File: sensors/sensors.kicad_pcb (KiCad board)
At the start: 2 copper layers, 75 x 56 mm, 69 parts, among them J1 GPIO, J3 JP_PWM, J4 JP_ADC, J5 JP_GPS, J6 JP_RADIO, J7 JP_RCIN, SW1 SW_SPDT_321, U1 SC16IS752IPW, U2 PCA9685PW, U3 ICM-42605, U4 IST8310, U5 MS5611-01BA, U6 74LVC1G86, U7 ADS1115IDGS, Y1 14.7456MHz, Y2 ASE-xxxMHz

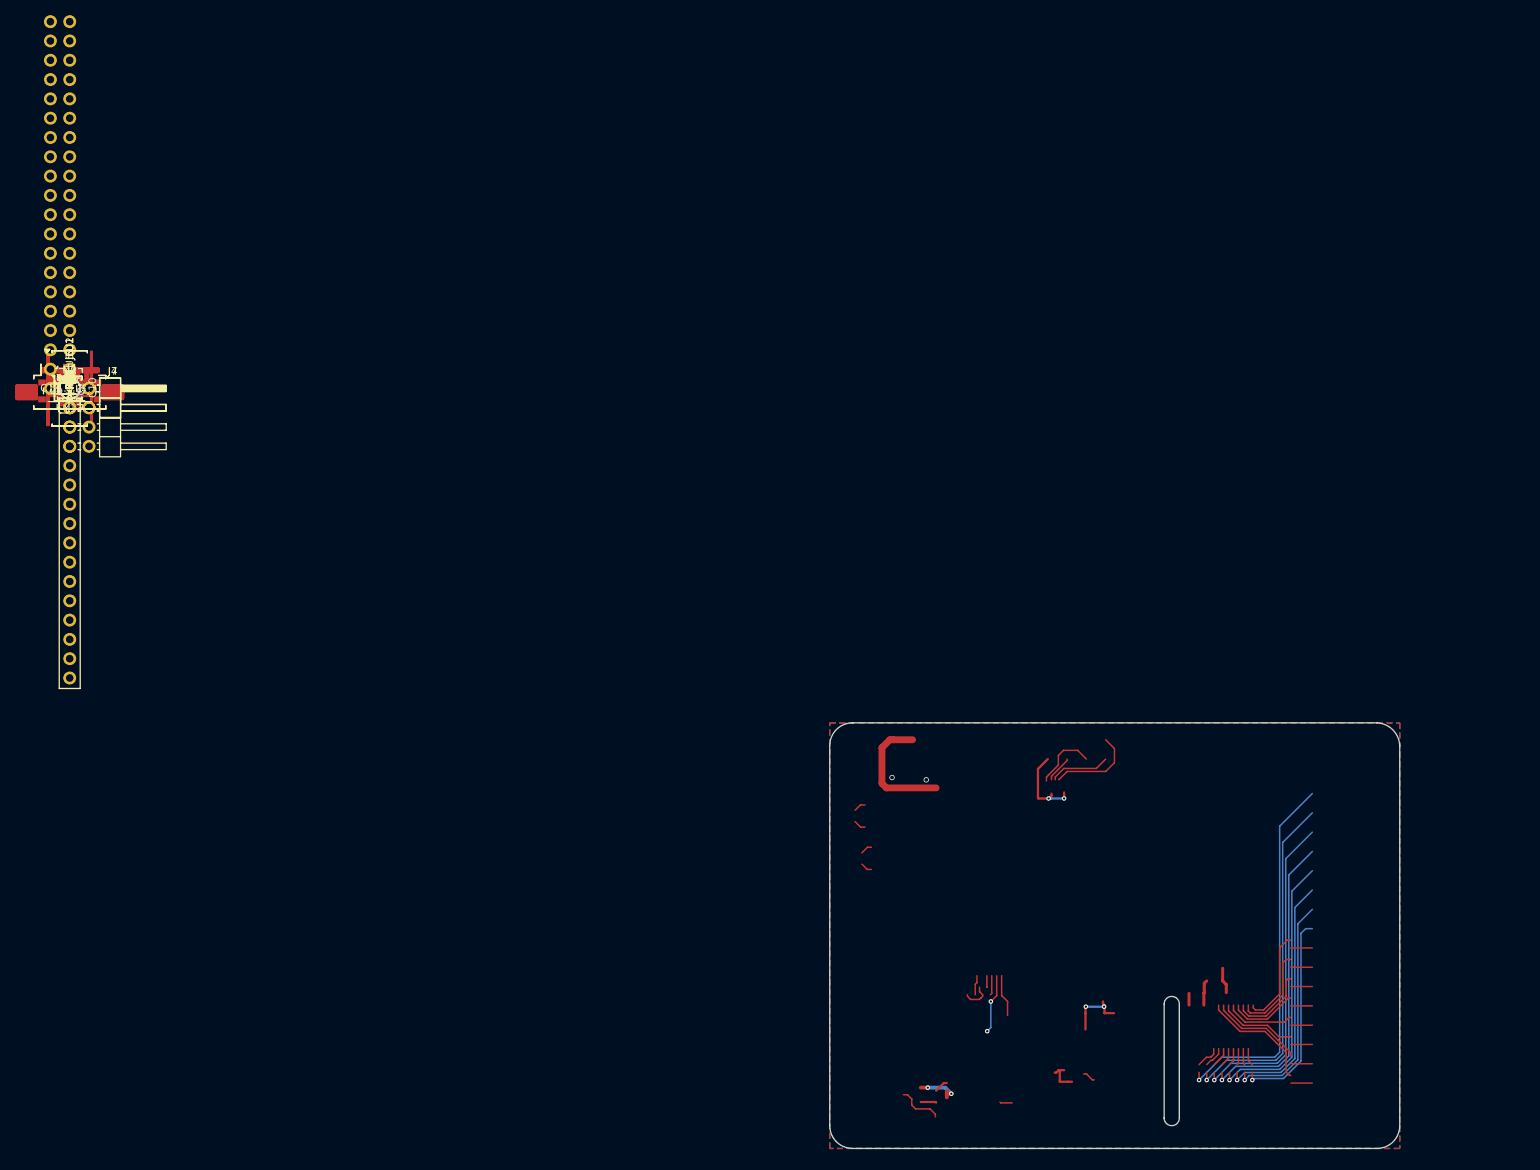
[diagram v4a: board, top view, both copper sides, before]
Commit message: add boot mode switch
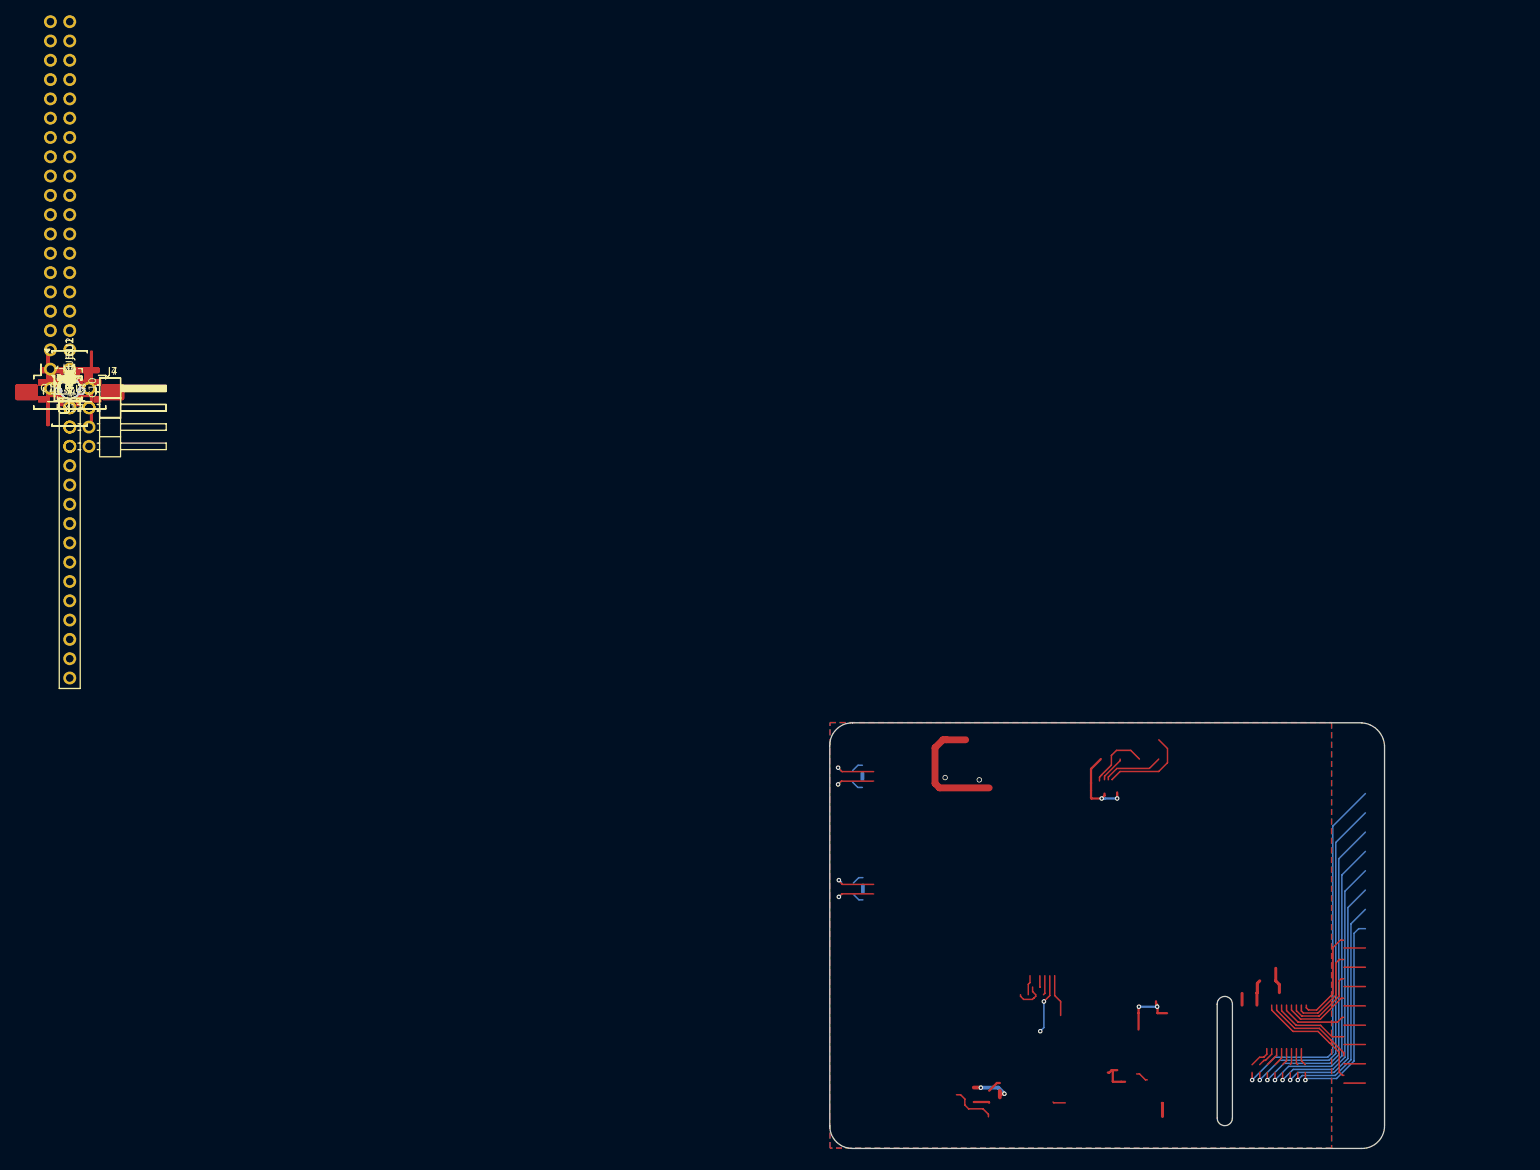
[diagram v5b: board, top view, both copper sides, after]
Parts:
- added R33, R34: 3.3KΩ (3301) ±1%, Resistor_SMD:R_0402_1005Metric, F.Cu at (0.00, 0.00)
- added R35: 10KΩ (1002) ±1%, Resistor_SMD:R_0402_1005Metric, F.Cu at (0.00, 0.00)
- added SW2: SW_SPDT_321, Button_Switch_SMD:SW_SPDT_PCM12, F.Cu at (0.00, 0.00)
- D1: value TXA_RED -> RXA_GREEN; moved to B.Cu
- D2: value RXA_GREEN -> TXA_RED; moved to B.Cu
- D3: value TXB_RED -> RXB_GREEN; moved to B.Cu
- D4: value RXB_GREEN -> TXB_RED; moved to B.Cu
- R11, R6, R8, R9: moved to B.Cu
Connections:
- D1 pad 1: /UART/TXA -> /UART/RXA
- D2 pad 1: /UART/RXA -> /UART/TXA
- D3 pad 1: /UART/TXB -> /UART/RXB
- D4 pad 1: /UART/RXB -> /UART/TXB
- J1 pad 35: /SPIMISO/GPIO19/PCM.FS -> /SPI1MISO/GPIO19/PCM.FS
- R10 pad 2: /UART/RXB -> /UART/TXB
- R7 pad 2: /UART/RXA -> /UART/TXA
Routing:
- net /UART/TXB: track 0.00 -> 5.42 mm, vias 0 -> 1
- net /UART/TXA: track 0.00 -> 5.40 mm, vias 0 -> 1
- net /UART/RXB: track 0.00 -> 5.30 mm, vias 0 -> 1
- net /UART/RXA: track 1.53 -> 6.74 mm, vias 0 -> 1
- net +3V3: track 37.6 -> 39.4 mm
- net Net-(SW2-C): track 0.00 -> 1.76 mm
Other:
- board size 75 x 56 mm -> 73 x 56 mm

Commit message: routing
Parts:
- removed J7: JP_RCIN, Connector_PinHeader_2.54mm:PinHeader_2x02_P2.54mm_Horizontal
- D1: value RXA_GREEN -> TXA_RED; moved to F.Cu
- D2: value TXA_RED -> RXA_GREEN; moved to F.Cu
- D3: value RXB_GREEN -> TXB_RED; moved to F.Cu
- D4: value TXB_RED -> RXB_GREEN; moved to F.Cu
- J4: footprint Connector_PinHeader_2.54mm:PinHeader_2x04_P2.54mm_Horizontal -> Connector_PinHeader_2.54mm:PinHeader_2x06_P2.54mm_Horizontal
- R11, R6, R8, R9: moved to F.Cu
- R33, R34: moved to B.Cu
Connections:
- D1 pad 1: /UART/RXA -> /UART/TXA
- D2 pad 1: /UART/TXA -> /UART/RXA
- D3 pad 1: /UART/RXB -> /UART/TXB
- D4 pad 1: /UART/TXB -> /UART/RXB
- J4 pad 1: GND -> /ADC/AIN0
- J4 pad 3: GND -> /ADC/AIN1
- J4 pad 5: /ADC/AIN3 -> /ADC/AIN2
- J4 pad 6: /ADC/AIN2 -> GND
- J4 pad 7: /ADC/AIN1 -> /ADC/AIN3
- J4 pad 8: /ADC/AIN0 -> GND
- R10 pad 2: /UART/TXB -> /UART/RXB
- R7 pad 2: /UART/TXA -> /UART/RXA
- U6 pad 1: /RC inverter/RC -> /RCIN
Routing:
- net /GPIO3/SCL1: track 0.00 -> 110.1 mm, vias 0 -> 2
- net /GPIO2/SDA1: track 0.00 -> 107.7 mm, vias 0 -> 4
- net /GPIO15/RXD0: track 2.07 -> 56.7 mm, vias 0 -> 3
- net /GPIO25: track 0.00 -> 54.3 mm, vias 0 -> 1
- net /SDIODAT0/GPIO24: track 0.00 -> 39.5 mm, vias 0 -> 1
- net /UART/TXB: track 5.42 -> 23.2 mm, vias 1 -> 2
- net /UART/RXB: track 5.30 -> 23.0 mm, vias 1 -> 2
- net +3V3: track 39.4 -> 53.0 mm, vias 6 -> 7
- net /RCIN: track 0.00 -> 12.7 mm, vias 0 -> 1
- net /ADC/AIN0: track 0.00 -> 10.0 mm, vias 0 -> 1
- net +5V: track 18.1 -> 27.2 mm
- net /ADC/AIN2: track 0.00 -> 8.45 mm
- net /ADC/AIN1: track 0.00 -> 7.91 mm, vias 0 -> 1
- net /ADC/AIN3: track 0.00 -> 6.37 mm
- net /UART/TXA: track 5.40 -> 10.9 mm, vias 1 -> 0
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
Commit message: intermediate commit
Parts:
- removed C12: 100nF (104) 10% 16V, Capacitor_SMD:C_0402_1005Metric
- removed R32: 10KΩ (1002) ±1%, Resistor_SMD:R_0402_1005Metric
- removed U7: ADS1115IDGS, Package_SO:TSSOP-10_3x3mm_P0.5mm
- added BZ1: Buzzer, Buzzer_Beeper:MagneticBuzzer_PUI_AT-0927-TT-6-R, F.Cu at (0.00, 0.00)
- added D6: 1N4148W, Diode_SMD:D_SOD-123, F.Cu at (0.00, 0.00)
- added Q1: SS8050, Package_TO_SOT_SMD:SOT-23, F.Cu at (0.00, 0.00)
- added R36: 1KΩ (1001) ±1%, Resistor_SMD:R_0402_1005Metric, F.Cu at (0.00, 0.00)
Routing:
- net +5V: track 27.2 -> 67.5 mm, vias 0 -> 2
- net /UART/TXA: track 10.9 -> 32.8 mm, vias 0 -> 5
- net /UART/CTSA: track 2.60 -> 24.1 mm, vias 0 -> 4
- net /UART/RTSA: track 0.00 -> 20.0 mm, vias 0 -> 2
- net /UART/RXA: track 11.6 -> 31.6 mm, vias 0 -> 5
- net /UART/RTSB: track 0.00 -> 17.3 mm, vias 0 -> 2
- net /UART/CTSB: track 1.45 -> 18.5 mm, vias 0 -> 2
- net /GPIO3/SCL1: track 110.1 -> 93.5 mm
- net /GPIO2/SDA1: track 107.7 -> 92.7 mm
- net /ADC/AIN0: track 10.0 -> 0.00 mm, vias 1 -> 0
- net /ADC/AIN2: track 8.45 -> 0.00 mm
- net /ADC/AIN1: track 7.91 -> 0.00 mm, vias 1 -> 0
- net /ADC/AIN3: track 6.37 -> 0.00 mm
- net +3V3: track 53.0 -> 51.3 mm
- net /RCIN: track 12.7 -> 14.2 mm
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
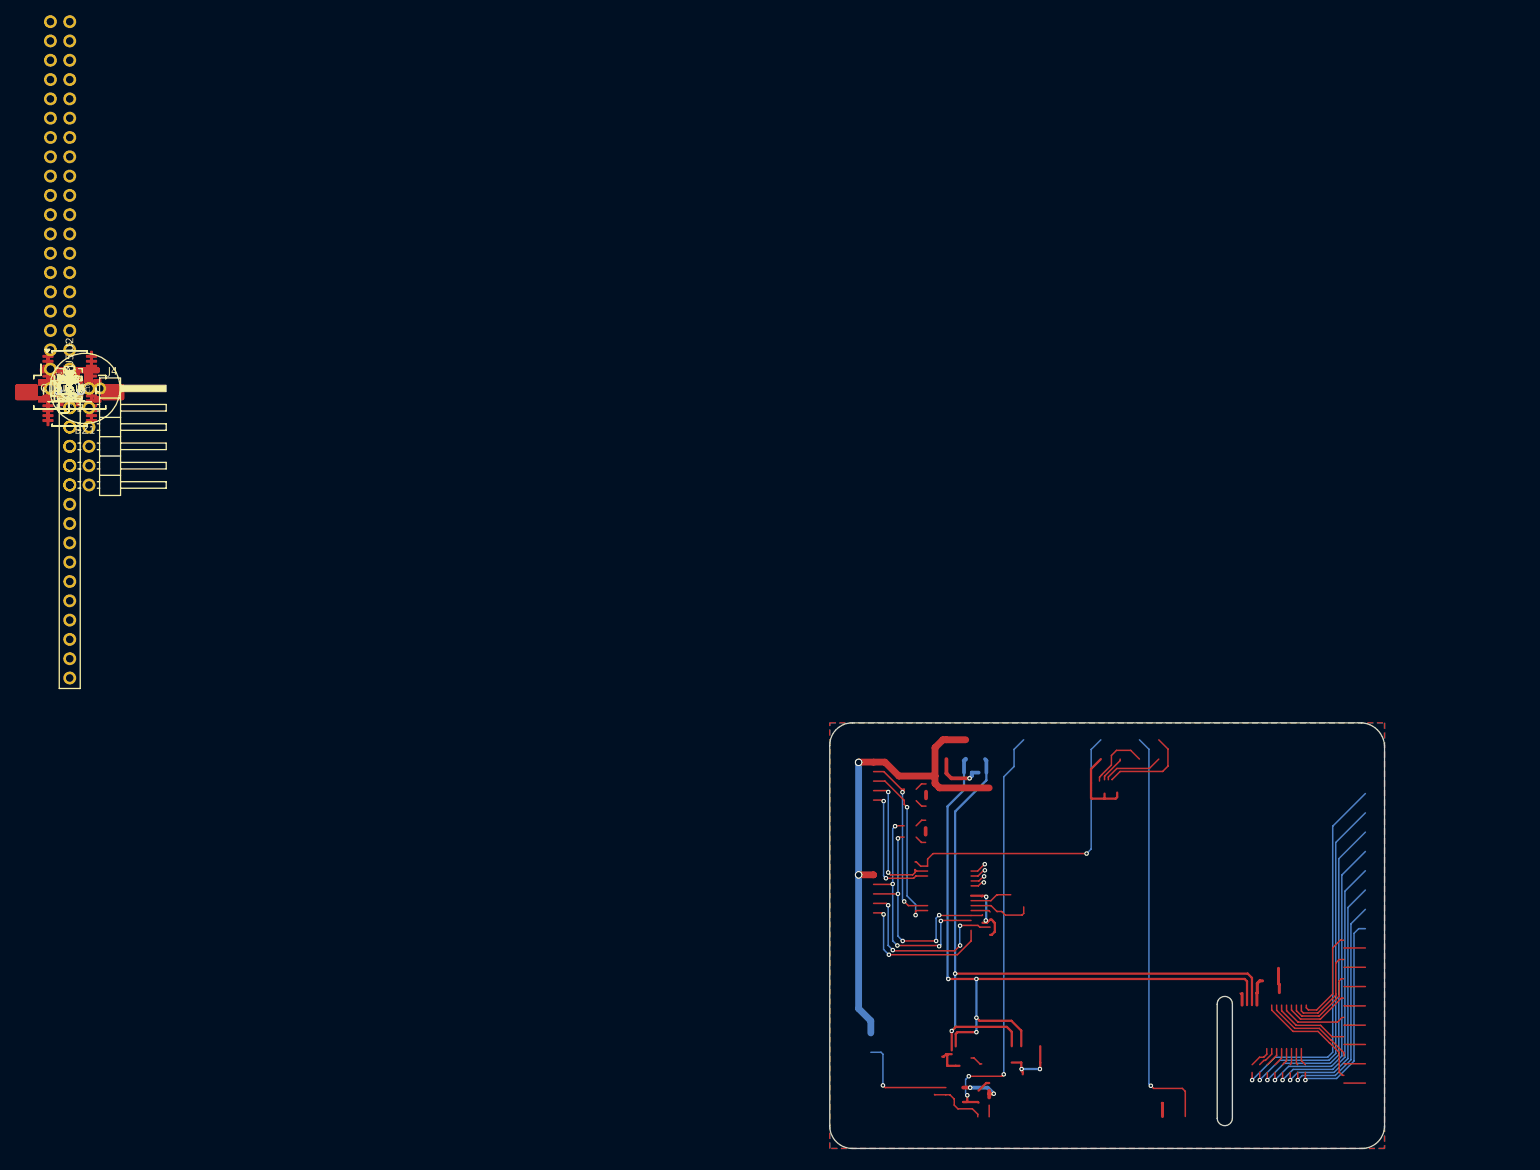
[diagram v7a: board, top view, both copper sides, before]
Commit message: manual downgrade to KiCAD 10.0
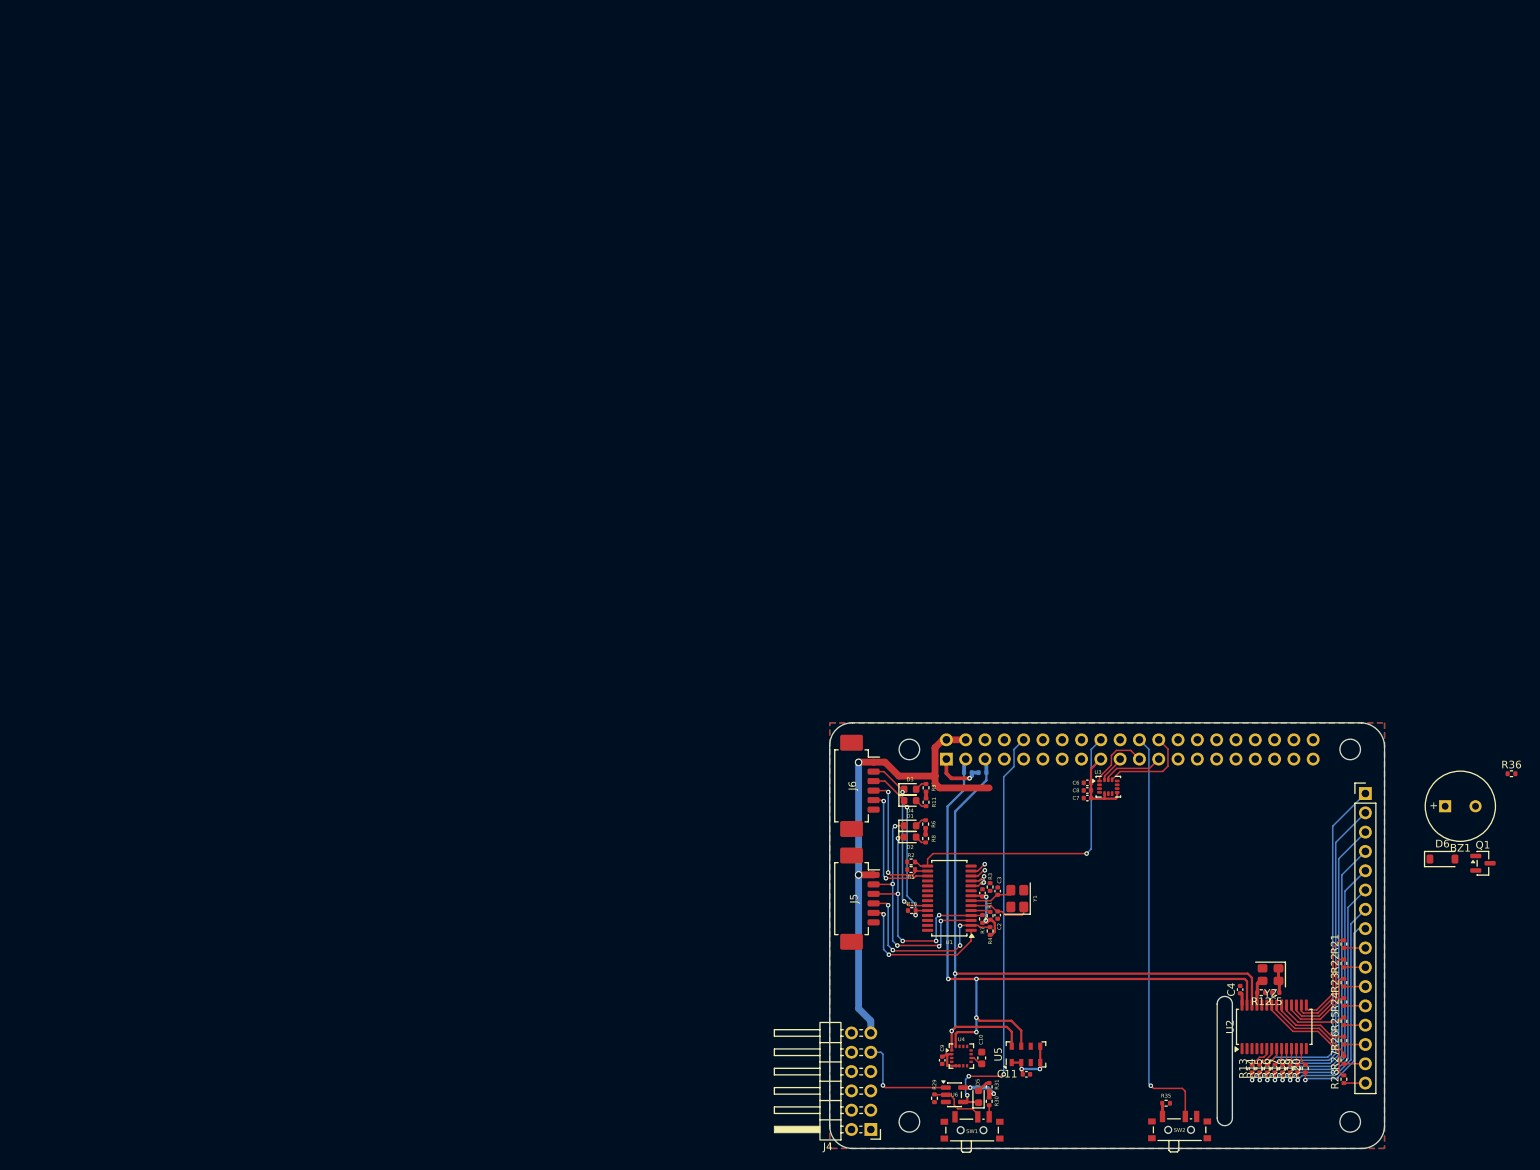
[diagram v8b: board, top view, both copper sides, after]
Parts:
- moved R36 196.4 mm to (189.7, 50.7)
- moved Q1 196.2 mm to (185.9, 62.5)
- moved MH4 194.2 mm to (168.5, 96.5)
- moved D6 190.9 mm to (180.6, 61.9)
- moved R28 190.7 mm to (167.7, 90.9), turned to 90 degrees
- moved R27 189.5 mm to (167.7, 88.3), turned to 90 degrees
- moved BZ1 189.1 mm to (181.0, 55.0)
- moved R26 188.3 mm to (167.7, 85.8), turned to 90 degrees
- moved R25 187.2 mm to (167.7, 83.3), turned to 90 degrees
- moved R24 186.1 mm to (167.7, 80.7), turned to 90 degrees
- moved R20 185.6 mm to (162.6, 89.5), turned to 90 degrees
- moved R23 185.0 mm to (167.7, 78.2), turned to 90 degrees
- moved R19 184.7 mm to (161.6, 89.5), turned to 90 degrees
- moved R22 183.9 mm to (167.7, 75.6), turned to 90 degrees
- moved R18 183.8 mm to (160.6, 89.5), turned to 90 degrees
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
